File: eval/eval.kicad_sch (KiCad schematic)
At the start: 1 part, among them U1 STM32G031G8U6

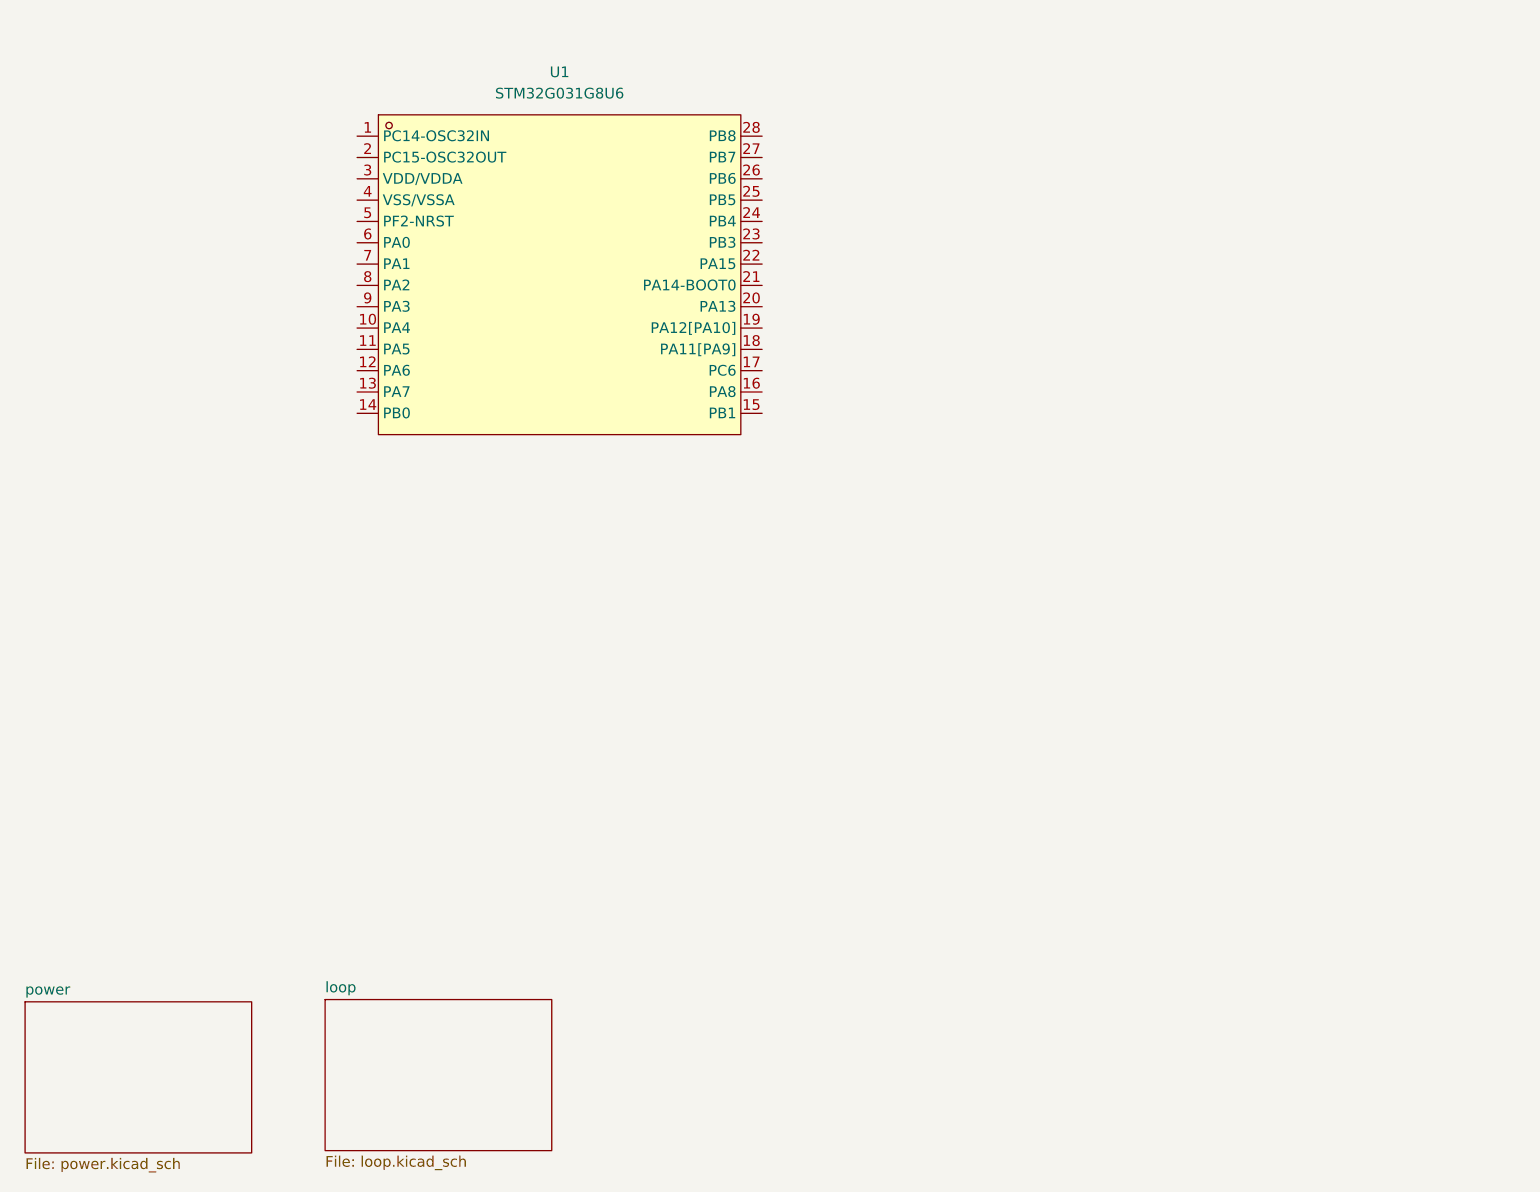
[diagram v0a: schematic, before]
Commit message: Change from G071 to G0B1, add screen, usb
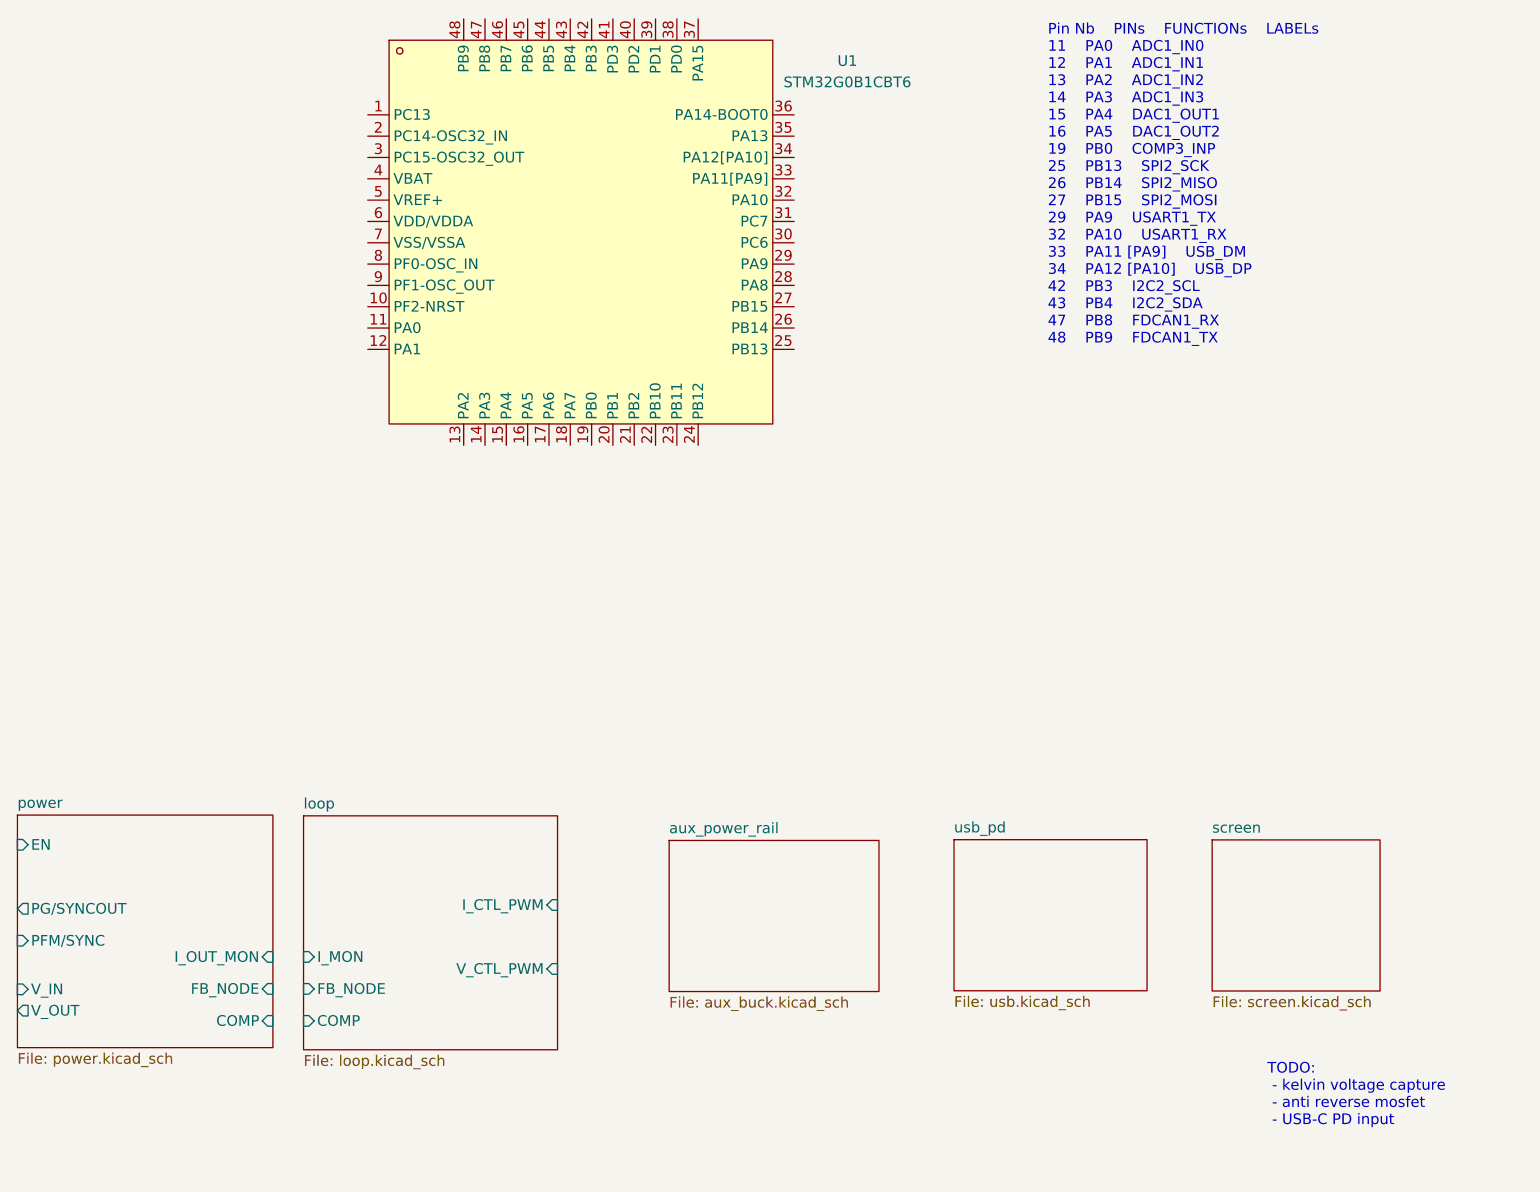
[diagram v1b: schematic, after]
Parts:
- removed U1: STM32G031G8U6, EasyEDA:UFQFPN-28_L4.0-W4.0-P0.50-BL, symbol charger:STM32G031G8U6
- added U1: STM32G0B1CBT6, EasyEDA:LQFP-48_L7.0-W7.0-P0.50-LS9.0-BL, symbol EasyEDA:STM32G0B1CBT6
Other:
- added sheet aux_power_rail (aux_buck.kicad_sch)
- added sheet screen (screen.kicad_sch)
- added sheet usb_pd (usb.kicad_sch)
- sheet loop ports: added COMP, FB_NODE, I_CTL_PWM, I_MON, V_CTL_PWM; removed none
- sheet power ports: added COMP, EN, FB_NODE, I_OUT_MON, PFM/SYNC, PG/SYNCOUT, V_IN, V_OUT; removed none
- note added: "Pin Nb PINs FUNCTIONs LABELs 11 PA0 ADC1_IN0 12 PA1 ADC1_IN1 13 PA2 ADC1_IN2 14 PA3 ADC1_IN3 15 PA4 DAC1_OUT1 16 PA5 DAC1_OUT2 19 PB0 COMP3_INP 25 PB13 SPI2_SCK 26 PB14 SPI2_MISO 27 PB15 SPI2_MOSI 29 PA9 USART1_TX 32 PA10 USART1_RX 33 PA11 [PA9] USB_DM 34 PA12 [PA10] USB_DP 42 PB3 I2C2_SCL 43 PB4 I2C2_SDA 47 PB8 FDCAN1_RX 48 PB9 FDCAN1_TX"
- note added: "TODO: - kelvin voltage capture - anti reverse mosfet - USB-C PD input"

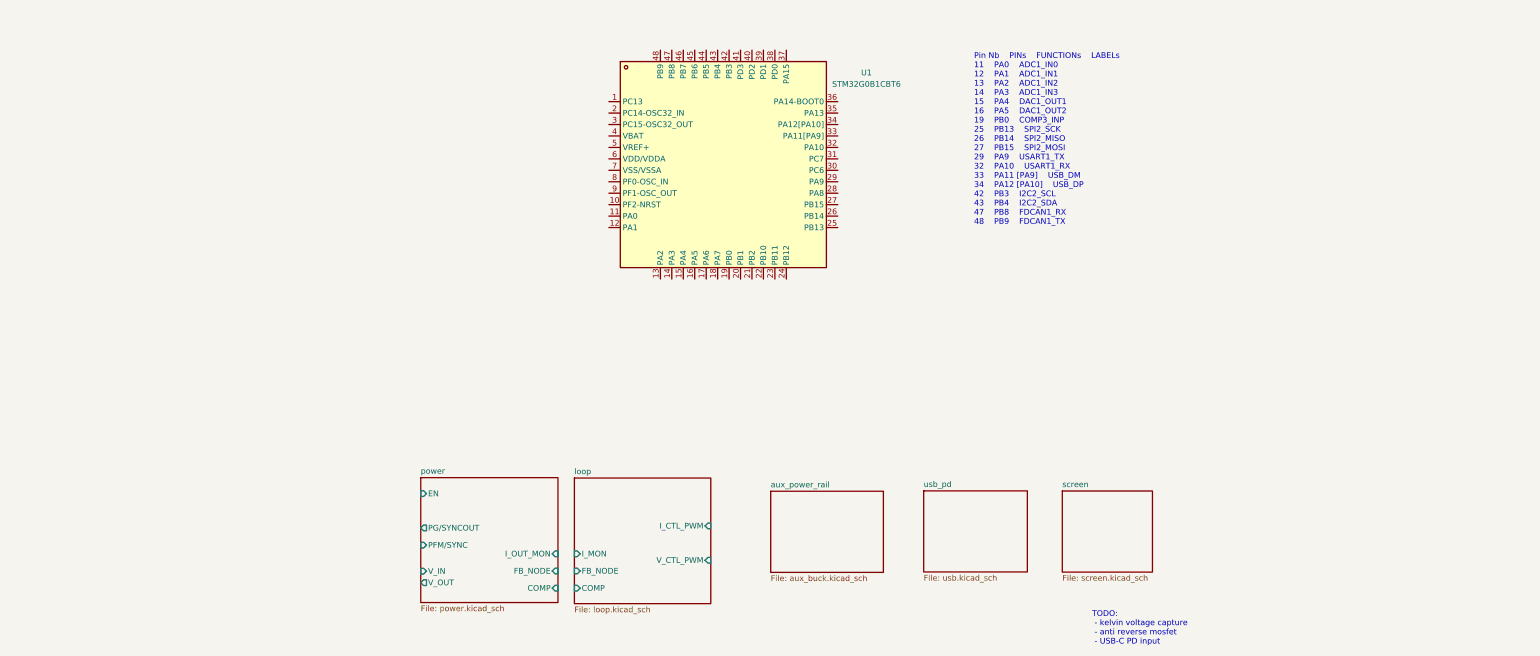
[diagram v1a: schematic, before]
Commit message: Complete most MCU pinout setup
next step power rail and pd
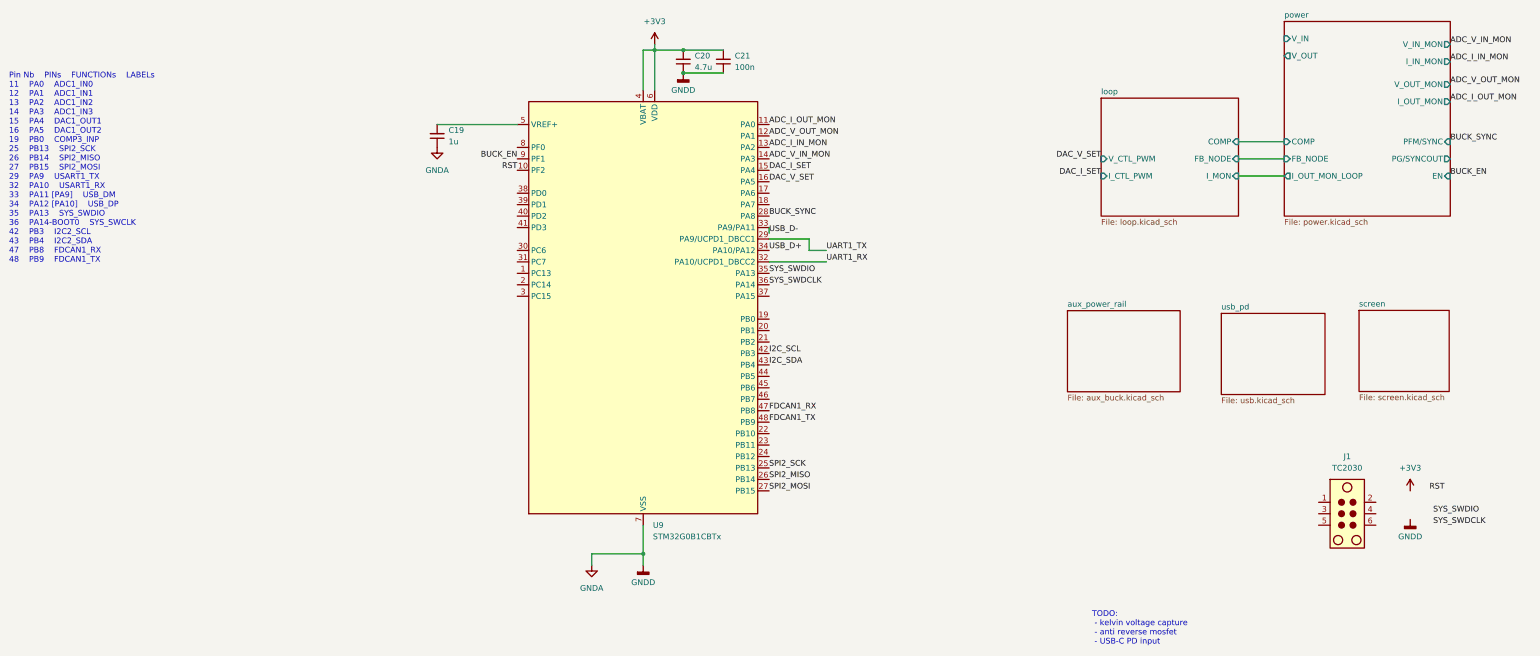
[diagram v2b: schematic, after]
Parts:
- removed U1: STM32G0B1CBT6, EasyEDA:LQFP-48_L7.0-W7.0-P0.50-LS9.0-BL, symbol EasyEDA:STM32G0B1CBT6
- added C19: 1u, symbol Device:C_Small
- added C20: 4.7u, symbol Device:C_Small
- added C21: 100n, symbol Device:C_Small
- added J1: TC2030, Connector:Tag-Connect_TC2030-IDC-NL_2x03_P1.27mm_Vertical, symbol Connector:TC2030
- added U9: STM32G0B1CBTx, Package_QFP:LQFP-48_7x7mm_P0.5mm, symbol MCU_ST_STM32G0:STM32G0B1CBTx
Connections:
- new net: C19.2, U9.5 (VREF+)
- new net +3V3: C20.2, C21.2, U9.4 (VBAT), U9.6 (VDD)
- new net ADC_I_IN_MON: U9.13 (PA2)
- new net ADC_I_OUT_MON: U9.11 (PA0)
- new net ADC_V_IN_MON: U9.14 (PA3)
- new net ADC_V_OUT_MON: U9.12 (PA1)
- new net BUCK_EN: U9.9 (PF1)
- new net BUCK_SYNC: U9.28 (PA8)
- new net DAC_I_SET: U9.15 (PA4)
- new net DAC_V_SET: U9.16 (PA5)
- new net FDCAN1_RX: U9.47 (PB8)
- new net FDCAN1_TX: U9.48 (PB9)
- new net GNDA: C19.1, C20.1, C21.1, U9.7 (VSS)
- new net I2C_SCL: U9.42 (PB3)
- new net I2C_SDA: U9.43 (PB4)
- new net RST: U9.10 (PF2)
- new net SPI2_MISO: U9.26 (PB14)
- new net SPI2_MOSI: U9.27 (PB15)
- new net SPI2_SCK: U9.25 (PB13)
- new net SYS_SWDCLK: U9.36 (PA14)
- new net SYS_SWDIO: U9.35 (PA13)
- new net UART1_RX: U9.32 (PA10/UCPD1_DBCC2)
- new net UART1_TX: U9.29 (PA9/UCPD1_DBCC1)
- new net USB_D+: U9.34 (PA10/PA12)
- new net USB_D-: U9.33 (PA9/PA11)
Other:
- sheet power ports: added I_IN_MON, I_OUT_MON_LOOP, V_IN_MON, V_OUT_MON; removed none
- note added: "Pin Nb PINs FUNCTIONs LABELs 11 PA0 ADC1_IN0 12 PA1 ADC1_IN1 13 PA2 ADC1_IN2 14 PA3 ADC1_IN3 15 PA4 DAC1_OUT1 16 PA5 DAC1_OUT2 19 PB0 COMP3_INP 25 PB13 SPI2_SCK 26 PB14 SPI2_MISO 27 PB15 SPI2_MOSI 29 PA9 USART1_TX 32 PA10 USART1_RX 33 PA11 [PA9] USB_DM 34 PA12 [PA10] USB_DP 35 PA13 SYS_SWDIO 36 PA14-BOOT0 SYS_SWCLK 42 PB3 I2C2_SCL 43 PB4 I2C2_SDA 47 PB8 FDCAN1_RX 48 PB9 FDCAN1_TX"
- note removed: "Pin Nb PINs FUNCTIONs LABELs 11 PA0 ADC1_IN0 12 PA1 ADC1_IN1 13 PA2 ADC1_IN2 14 PA3 ADC1_IN3 15 PA4 DAC1_OUT1 16 PA5 DAC1_OUT2 19 PB0 COMP3_INP 25 PB13 SPI2_SCK 26 PB14 SPI2_MISO 27 PB15 SPI2_MOSI 29 PA9 USART1_TX 32 PA10 USART1_RX 33 PA11 [PA9] USB_DM 34 PA12 [PA10] USB_DP 42 PB3 I2C2_SCL 43 PB4 I2C2_SDA 47 PB8 FDCAN1_RX 48 PB9 FDCAN1_TX"

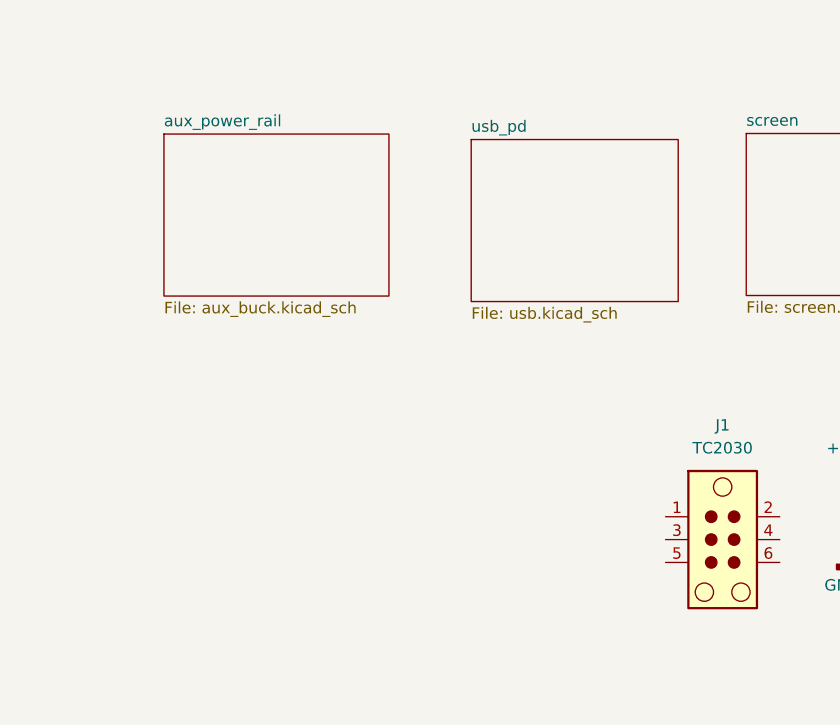
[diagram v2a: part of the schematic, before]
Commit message: Complete first complete draft sch (add screen spi and back light cc)
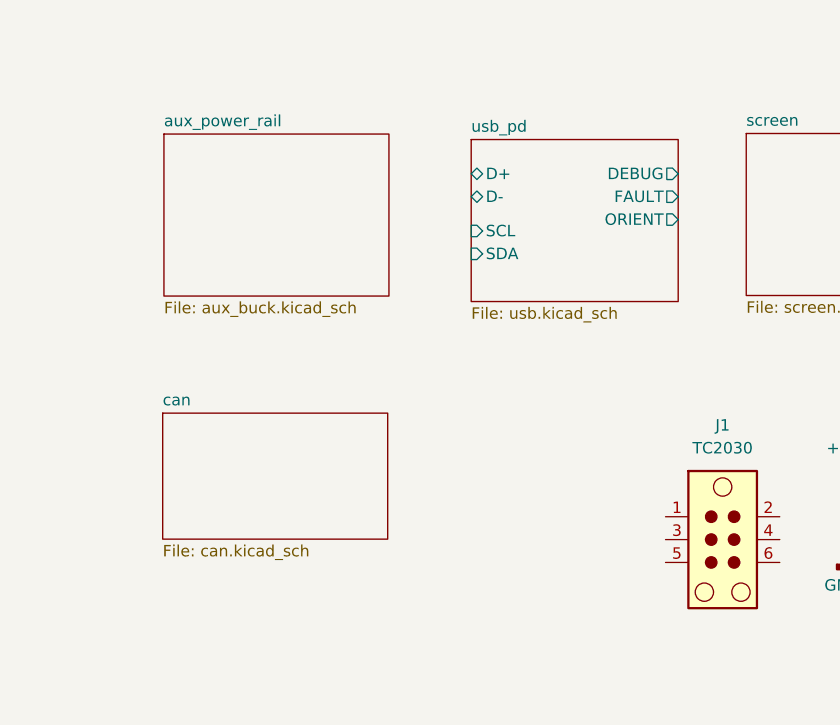
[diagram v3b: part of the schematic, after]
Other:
- added sheet can (can.kicad_sch)
- sheet usb_pd ports: added D+, D-, DEBUG, FAULT, ORIENT, SCL, SDA; removed none
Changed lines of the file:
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@@
+	)
+	(sheet
+		(at 174 132)
+		(size 25 14)
+		(exclude_from_sim no)
+		(in_bom yes)
+		(on_board yes)
+		(dnp no)
+		(fields_autoplaced yes)
+		(stroke
+			(width 0.1524)
+			(type solid)
+		)
+		(fill
+			(color 0 0 0 0)
+		)
+		(property "Sheetname" "can"
+			(at 174 131.2884 0)
+			(show_name no)
+			(do_not_autoplace no)
+			(effects
+				(font
+					(size 1.27 1.27)
+				)
+				(justify left bottom)
+			)
+		)
+		(property "Sheetfile" "can.kicad_sch"
+			(at 174 146.5846 0)
+			(show_name no)
+			(do_not_autoplace no)
+			(effects
+				(font
+					(size 1.27 1.27)
+				)
+				(justify left top)
+			)
+		)
+		(instances
+			(project "eval"
+				(path "/8b023652-20db-48ce-ad53-bc2d9a4e5dd4"
+					(page "7")
+				)
+			)
+		)
 	)
 	(sheet
@@
 			)
 		)
+		(pin "D+" bidirectional
+			(at 208.28 105.41 180)
+			(effects
+				(font
+					(size 1.27 1.27)
+				)
+				(justify left)
+			)
+		)
+		(pin "D-" bidirectional
+			(at 208.28 107.95 180)
+			(effects
+				(font
+					(size 1.27 1.27)
+				)
+				(justify left)
+			)
+		)
+		(pin "DEBUG" output
+			(at 231.28 105.41 0)
+			(effects
+				(font
+					(size 1.27 1.27)
+				)
+				(justify right)
+			)
+		)
+		(pin "FAULT" output
+			(at 231.28 107.95 0)
+			(effects
+				(font
+					(size 1.27 1.27)
+				)
+				(justify right)
+			)
+		)
+		(pin "ORIENT" output
+			(at 231.28 110.49 0)
+			(effects
+				(font
+					(size 1.27 1.27)
+				)
+				(justify right)
+			)
+		)
+		(pin "SCL" input
+			(at 208.28 111.76 180)
+			(effects
+				(font
+					(size 1.27 1.27)
+				)
+				(justify left)
+			)
+		)
+		(pin "SDA" input
+			(at 208.28 114.3 180)
+			(effects
+				(font
+					(size 1.27 1.27)
+				)
+				(justify left)
+			)
+		)
